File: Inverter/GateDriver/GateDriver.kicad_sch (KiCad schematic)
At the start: 61 parts, among them IC1 HCPL-316J-500E, IC2 LM5185QPWPRQ1, J1 Conn_01x06_Pin, Q1 MJE3055TG, Q2 MJE2955TG, Q3 NMOS, T1 Transformer_1P_1S

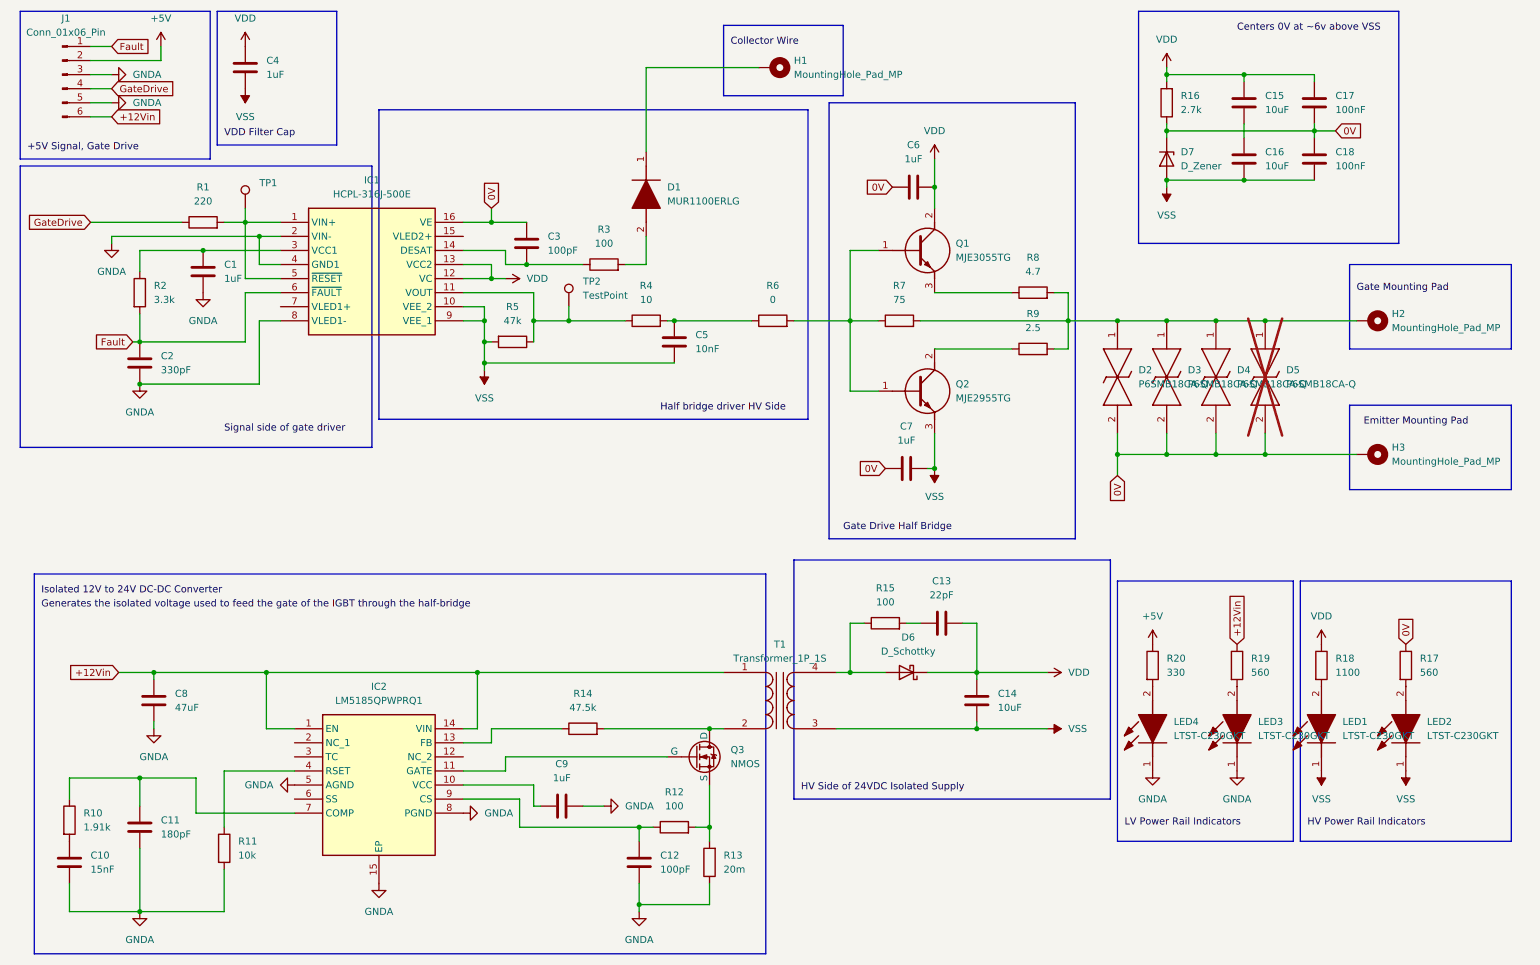
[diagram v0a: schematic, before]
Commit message: Update Schematics, Inverter, Gate Driver, Mechanical, Software
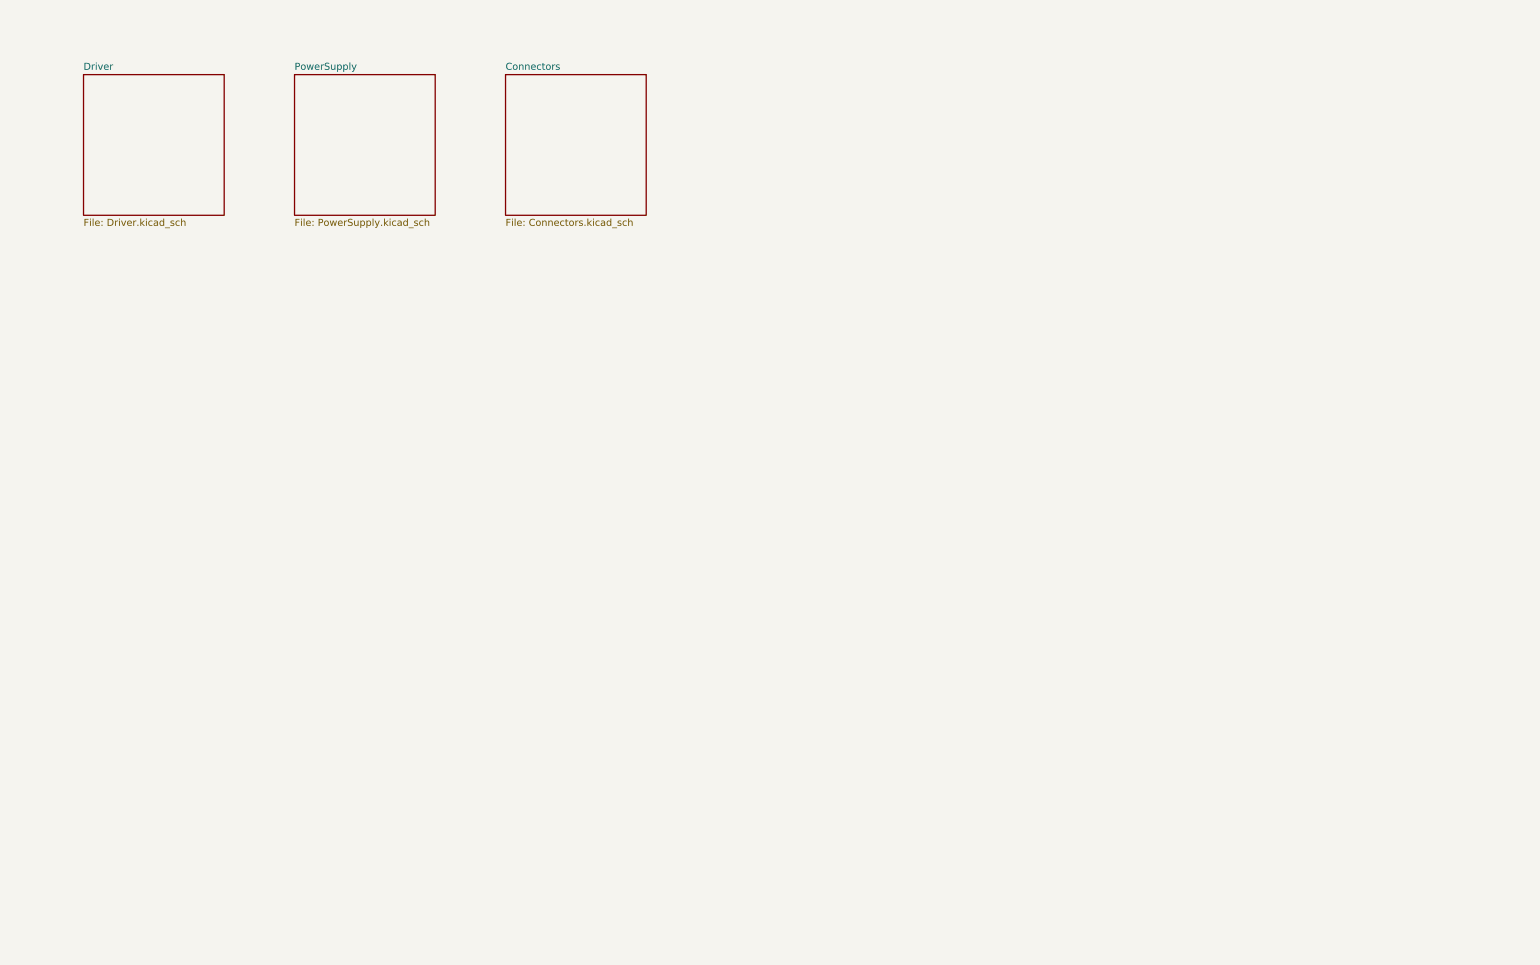
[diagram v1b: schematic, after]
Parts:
- removed C1, C4, C6, C7, C9: 1uF, symbol Device:C
- removed C10: 15nF, symbol Device:C
- removed C11: 180pF, symbol Device:C
- removed C12, C3: 100pF, symbol Device:C
- removed C13: 22pF, symbol Device:C
- removed C14, C15, C16: 10uF, symbol Device:C
- removed C17, C18: 100nF, symbol Device:C
- removed C2: 330pF, symbol Device:C
- removed C5: 10nF, symbol Device:C
- removed C8: 47uF, symbol Device:C
- removed D1: MUR1100ERLG, DIOAD1405W86L465D235, symbol InverterCom:MUR1100ERLG
- removed D2, D3, D4, D5: P6SMB18CA-Q, DIONM5443X244N, symbol InverterCom:P6SMB18CA-Q
- removed D6: D_Schottky, symbol Device:D_Schottky
- removed D7: D_Zener, symbol Device:D_Zener
- removed H1, H2, H3: MountingHole_Pad_MP, symbol Mechanical:MountingHole_Pad_MP
- removed IC1: HCPL-316J-500E, SOIC127P1036X391-16N, symbol InverterCom:HCPL-316J-500E
- removed IC2: LM5185QPWPRQ1, SOP65P640X120-15N, symbol InverterCom:LM5185QPWPRQ1
- removed J1: Conn_01x06_Pin, symbol Connector:Conn_01x06_Pin
- removed LED1, LED2, LED3, LED4: LTST-C230GKT, LEDC3216X120N, symbol InverterCom:LTST-C230GKT
- removed Q1: MJE3055TG, TO254P483X1010X2035-3P, symbol InverterCom:MJE3055TG
- removed Q2: MJE2955TG, TO254P483X1010X2035-3P, symbol InverterCom:MJE3055TG
- removed Q3: NMOS, symbol Simulation_SPICE:NMOS
- removed R1: 220, 1210, symbol Device:R
- removed R10: 1.91k, 1210, symbol Device:R
- removed R11: 10k, 1210, symbol Device:R
- removed R12, R15, R3: 100, 1210, symbol Device:R
- removed R13: 20m, 1210, symbol Device:R
- removed R14: 47.5k, 1210, symbol Device:R
- removed R16: 2.7k, 1210, symbol Device:R
- removed R17, R19: 560, 1210, symbol Device:R
- removed R18: 1100, 1210, symbol Device:R
- removed R2: 3.3k, 1210, symbol Device:R
- removed R20: 330, 1210, symbol Device:R
- removed R4: 10, 1210, symbol Device:R
- removed R5: 47k, 1210, symbol Device:R
- removed R6: 0, 1210, symbol Device:R
- removed R7: 75, 1210, symbol Device:R
- removed R8: 4.7, 1210, symbol Device:R
- removed R9: 2.5, 1210, symbol Device:R
- removed T1: Transformer_1P_1S, symbol Device:Transformer_1P_1S
- removed TP1: ~, symbol Connector:TestPoint
- removed TP2: TestPoint, symbol Connector:TestPoint
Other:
- added sheet Connectors (Connectors.kicad_sch)
- added sheet Driver (Driver.kicad_sch)
- added sheet PowerSupply (PowerSupply.kicad_sch)
